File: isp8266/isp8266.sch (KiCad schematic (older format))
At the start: 0 parts

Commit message: Complete power sch
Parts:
- added C? (x4): 10u, symbol Device:C_Small
- added C? (x6): 22u, symbol Device:C_Small
- added C? (x2): 1u, symbol Device:C_Small
- added D? (x2): LED_Small, symbol Device:LED_Small
- added L?: L_Small, symbol Device:L_Small
- added P?: USB_C_Plug, symbol Connector:USB_C_Plug
- added R? (x2): 5k1, symbol Device:R_Small
- added R?: 10k, symbol Device:R_Small
- added R?: 2, symbol Device:R_Small
- added R? (x2): 1k, symbol Device:R_Small
- added R?: 0.9, symbol Device:R_Small
- added SW?: SW_Push, symbol Switch:SW_Push
- added U?: ESP-12E, RF_Module:ESP-12E, symbol RF_Module:ESP-12E
- added U?: AP1117-33, Package_TO_SOT_SMD:SOT-223-3_TabPin2, symbol Regulator_Linear:AP1117-33
- added U?: IPS5306, symbol IPS5306:IPS5306
- added U?: CH340C, Package_SO:SOIC-16_3.9x9.9mm_P1.27mm, symbol Interface_USB:CH340C
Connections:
- new net: D?.2 (A), U?.2 (LED1)
- new net: R?.1, U?.3 (LED2), U?.4 (LED3)
- new net: SW?.1, U?.5 (KEY)
- new net: L?.1, U?.7 (SW)
- new net: P?.A5 (CC), R?.1
- new net: P?.B5 (VCONN), R?.1
- new net: R?.1, SW?.2
- new net: C?.1, R?.2
- new net: D?.1 (K), R?.1
- new net +3V3: C?.1, C?.1, D?.2 (A), U?.2 (VO)
- new net +5V: C?.1, C?.1, C?.1, C?.1, C?.1, C?.1, U?.3 (VI), U?.8 (VOUT)
- new net BAT: C?.1, L?.2, R?.1
- new net D+: P?.A6 (D+)
- new net D-: P?.A7 (D-)
- new net GND: C?.2, C?.2, C?.2, C?.2, C?.2, C?.2, C?.2, C?.2, C?.2, C?.2, C?.2, C?.2, D?.1 (K), P?.A1 (GND), P?.A10 (RX2-), P?.A11 (RX2+), P?.A12 (GND), P?.A2 (TX1+), P?.A3 (TX1-), P?.B1 (GND), P?.B10 (RX1-), P?.B11 (RX1+), P?.B12 (GND), P?.B2 (TX2+), P?.B3 (TX2-), P?.S1 (SHIELD), R?.2, R?.2, R?.2, R?.2, U?.1 (GND), U?.9 (GND)
- new net IC_BAT: C?.1, R?.2, R?.2, U?.6 (BAT)
- new net VBUS: C?.1, P?.A4 (VBUS), P?.A9 (VBUS), P?.B4 (VBUS), P?.B9 (VBUS), R?.1, U?.1 (VIN)
- no-connect marks 0 -> 2

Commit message: Complete all peripherals
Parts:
- added C? (x2): 100n, symbol Device:C_Small
- added C?: 10u, symbol Device:C_Small
- added C?: 470p, symbol Device:C_Small
- added C?: 100p, symbol Device:C_Small
- added J?: S0, symbol Connector_Generic:Conn_01x03
- added J?: S1, symbol Connector_Generic:Conn_01x03
- added J?: S2, symbol Connector_Generic:Conn_01x03
- added J?: S3, symbol Connector_Generic:Conn_01x03
- added J?: IMU, symbol Connector_Generic:Conn_01x04
- added J?: USART, symbol Connector_Generic:Conn_01x04
- added J?: F0, symbol Connector_Generic:Conn_01x02
- added J?: F1, symbol Connector_Generic:Conn_01x02
- added J?: BATTERY, symbol Connector_Generic:Conn_01x02
- added J?: I2C, symbol Connector_Generic:Conn_01x04
- added Q? (x2): S8050, Package_TO_SOT_THT:TO-92_Inline, symbol Transistor_BJT:S8050
- added Q? (x2): IRLML0030, Package_TO_SOT_SMD:SOT-23, symbol Transistor_FET:IRLML0030
- added R? (x2): 470, symbol Device:R_Small
- added R? (x6): 10k, symbol Device:R_Small
- added R? (x2): 4k7, symbol Device:R_Small
- added R? (x4): 1k, symbol Device:R_Small
- L?: value L_Small -> 1u
- R?: value 0.9 -> 0.5
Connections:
- net GND is gone; now on net -BATT: C?.2, C?.2, C?.2, C?.2, C?.2, C?.2, C?.2, C?.2, C?.2, C?.2, C?.2, C?.2, D?.1 (K), P?.A1 (GND), P?.A10 (RX2-), P?.A11 (RX2+), P?.A12 (GND), P?.A2 (TX1+), P?.A3 (TX1-), P?.B1 (GND), P?.B10 (RX1-), P?.B11 (RX1+), P?.B12 (GND), P?.B2 (TX2+), P?.B3 (TX2-), P?.S1 (SHIELD), R?.2, R?.2, R?.2, R?.2, U?.1 (GND), U?.9 (GND)
- net +3V3: now also U?.16 (VCC), U?.8 (VCC), C?.1, C?.1, C?.1, J?.1 (Pin_1), J?.1 (Pin_1), J?.1 (Pin_1), R?.2, R?.2, R?.2, R?.2
- net +5V: now also J?.1 (Pin_1), J?.1 (Pin_1), J?.1 (Pin_1), J?.1 (Pin_1)
- net D+: now also U?.5 (UD+)
- net D-: now also U?.6 (UD-)
- net RST: now reaches U?.1 (~RST)
- net RST: now also C?.2, Q?.3 (C), R?.1
- net -BATT: now reaches U?.15 (GND)
- net -BATT: now also U?.1 (GND), C?.1, C?.2, C?.2, C?.2, C?.2, J?.2 (Pin_2), J?.2 (Pin_2), J?.3 (Pin_3), J?.3 (Pin_3), J?.3 (Pin_3), J?.3 (Pin_3), J?.4 (Pin_4), J?.4 (Pin_4), Q?.2 (S), Q?.2 (S), R?.1, R?.1
- net GPIO15: now reaches U?.16 (GPIO15)
- net GPIO15: now also Q?.1 (G), R?.2
- net IO2: now reaches U?.17 (GPIO2)
- net IO2: now also R?.1, R?.2
- net IO0: now reaches U?.18 (GPIO0)
- net IO0: now also Q?.3 (C), R?.1, R?.2
- net SDA: now reaches U?.19 (GPIO4)
- net SDA: now also J?.2 (Pin_2), J?.4 (Pin_4)
- net SCL: now reaches U?.20 (GPIO5)
- net SCL: now also J?.3 (Pin_3), J?.3 (Pin_3)
- net TXD: now reaches U?.21 (GPIO3/RXD)
- net TXD: now also J?.3 (Pin_3), R?.1
- net RXD: now reaches U?.22 (GPIO1/TXD)
- net RXD: now also J?.2 (Pin_2), R?.1
- net EN: now reaches U?.3 (EN)
- net EN: now also R?.1
- net GPIO14: now reaches U?.5 (GPIO14)
- net GPIO14: now also Q?.1 (G), R?.2
- net GPIO12: now reaches U?.6 (GPIO12)
- net GPIO12: now also R?.2
- net GPIO13: now reaches U?.7 (GPIO13)
- net GPIO13: now also R?.2
- net at U?.13 (~DTR): now also Q?.1 (E), R?.1
- net at U?.14 (~RTS): now also Q?.1 (E), R?.1
- net at U?.2 (TXD): now also R?.2
- net at U?.3 (RXD): now also R?.2
- net at U?.4 (V3): now also C?.1
- net BAT renamed +BATT
- net +BATT: now also J?.1 (Pin_1), J?.1 (Pin_1), J?.1 (Pin_1)
- new net: Q?.2 (B), R?.2 (x2)
- new net: J?.2 (Pin_2), R?.1 (x4)
- new net: J?.2 (Pin_2), Q?.3 (D) (x2)
- no-connect marks 2 -> 15
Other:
- note added: "5V to 3V3"
- note added: "Battery"
- note added: "ESP8266"
- note added: "Fire"
- note added: "Peripherals"
- note added: "USB C Power Supply"
- note added: "USB TTL"
- moved on the sheet: C?, D?, L?, P?, R?, SW?, U?, U?A

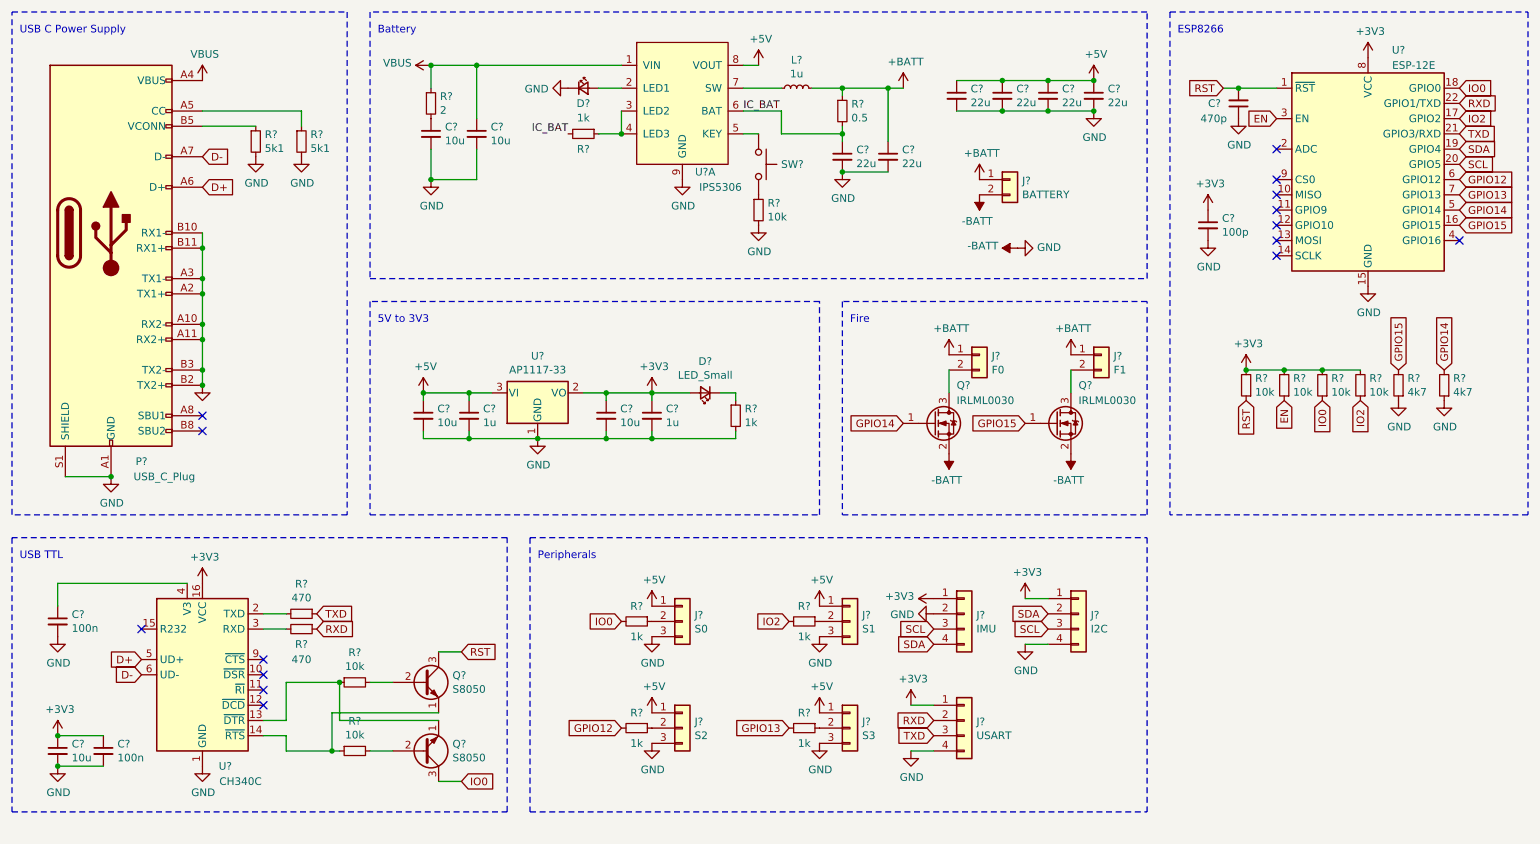
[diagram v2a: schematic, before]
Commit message: Annotate all symbols
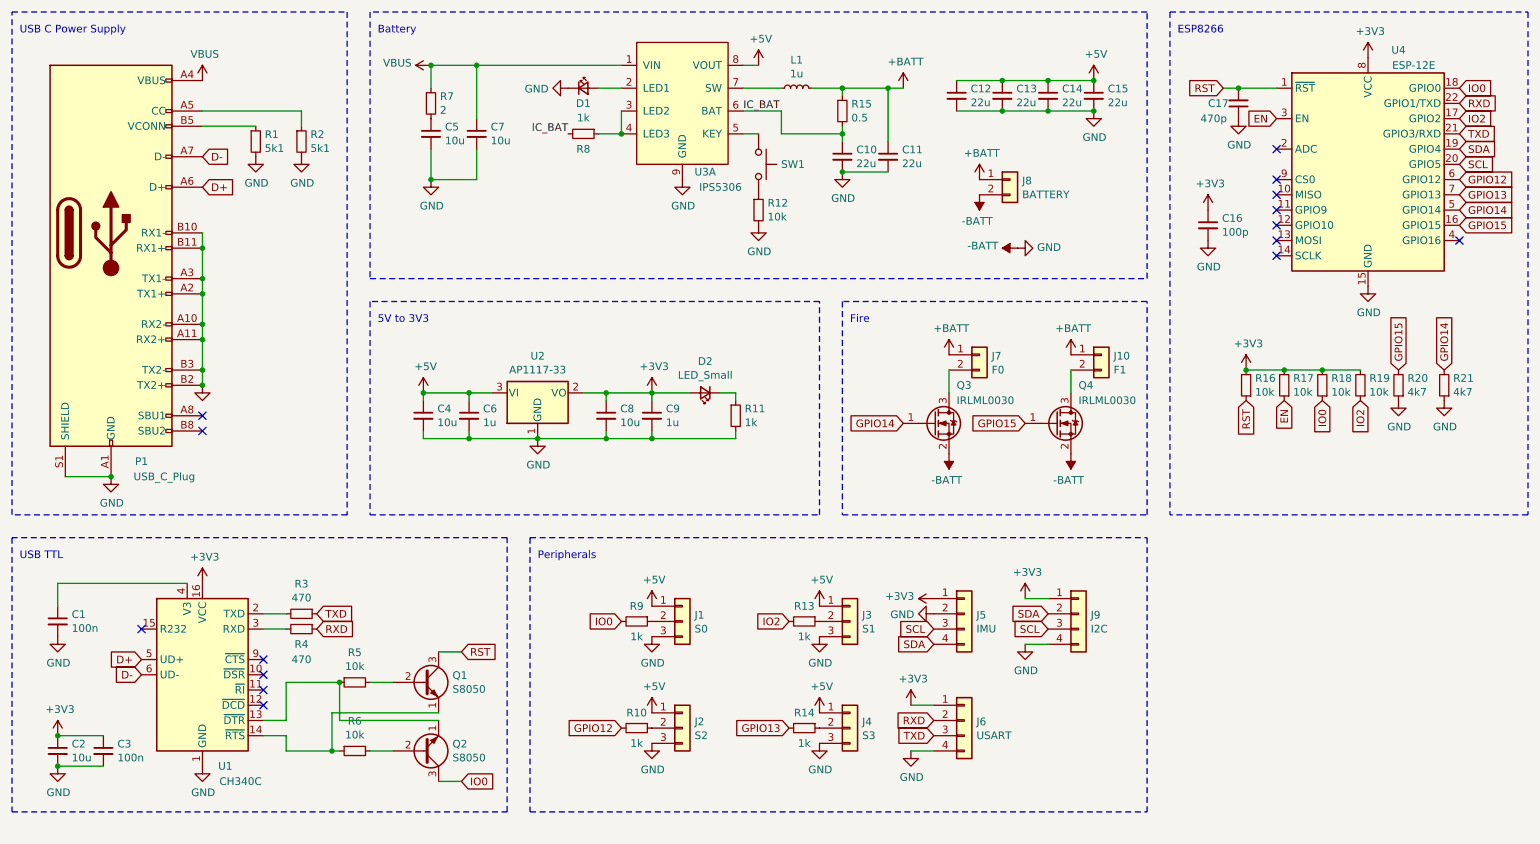
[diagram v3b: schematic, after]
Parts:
- gave numbers to parts that had none: 61

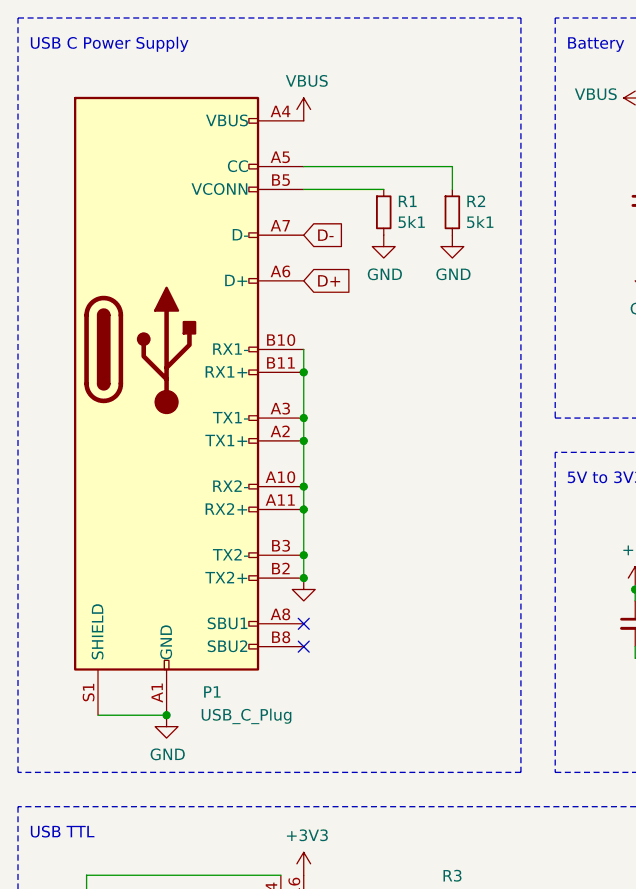
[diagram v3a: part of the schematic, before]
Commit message: Use USB_C_Receptacle
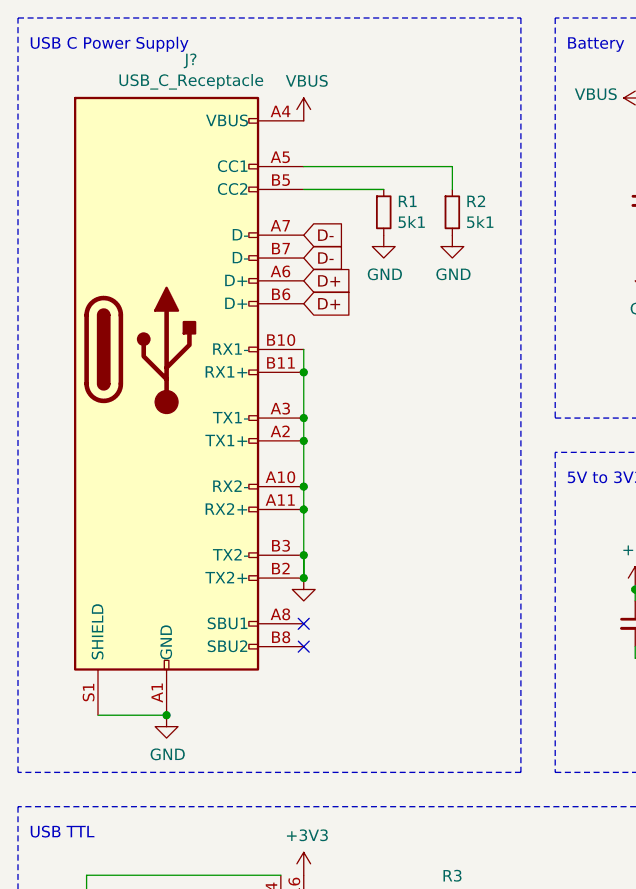
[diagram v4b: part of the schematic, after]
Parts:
- removed P1: USB_C_Plug, symbol Connector:USB_C_Plug
- added J?: USB_C_Receptacle, symbol Connector:USB_C_Receptacle
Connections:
- net -BATT: now also J?.A1 (GND), J?.A10 (RX2-), J?.A11 (RX2+), J?.A12 (GND), J?.A2 (TX1+), J?.A3 (TX1-), J?.B1 (GND), J?.B10 (RX1-), J?.B11 (RX1+), J?.B12 (GND), J?.B2 (TX2+), J?.B3 (TX2-), J?.S1 (SHIELD)
- net D+: now also J?.A6 (D+), J?.B6 (D+)
- net D-: now also J?.A7 (D-), J?.B7 (D-)
- net VBUS: now also J?.A4 (VBUS), J?.A9 (VBUS), J?.B4 (VBUS), J?.B9 (VBUS)
- net at R2.1: now also J?.A5 (CC1)
- net at R1.1: now also J?.B5 (CC2)
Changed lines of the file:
@@
 Comment4 ""
 $EndDescr
-$Comp
-L Connector:USB_C_Plug P1
-U 1 1 638029CF
-P 1300 2050
-F 0 "P1" H 1500 550 50  0000 C CNN
-F 1 "USB_C_Plug" H 1650 450 50  0000 C CNN
-F 2 "" H 1450 2050 50  0001 C CNN
-F 3 "https://www.usb.org/sites/default/files/documents/usb_type-c.zip" H 1450 2050 50  0001 C CNN
-	1    1300 2050
-	1    0    0    -1
-$EndComp
 Text GLabel 1900 1750 2    50   Input ~ 0
 D+
@@
 	1    0    0    -1
 $EndComp
-Connection ~ 1300 3650
-Wire Wire Line
-	1900 2050 1900 2150
-Connection ~ 1900 2150
-Wire Wire Line
-	1900 2150 1900 2350
-Connection ~ 1900 2350
-Wire Wire Line
-	1900 2350 1900 2450
-Connection ~ 1900 2450
-Wire Wire Line
-	1900 2450 1900 2650
-Connection ~ 1900 2650
-Wire Wire Line
-	1900 2650 1900 2750
-Connection ~ 1900 2750
-Wire Wire Line
-	1900 2750 1900 2950
-Connection ~ 1900 2950
-Wire Wire Line
-	1900 2950 1900 3050
 $Comp
 L Device:R_Small R1
@@
 	1    0    0    -1
 $EndComp
-Connection ~ 1900 3050
 NoConn ~ 1900 3250
 NoConn ~ 1900 3350
@@
 $EndComp
 $Comp
+L power:GND #PWR01
+U 1 1 63C8E842
+P 950 4700
+F 0 "#PWR01" H 950 4450 50  0001 C CNN
+F 1 "GND" H 955 4527 50  0000 C CNN
+F 2 "" H 950 4700 50  0001 C CNN
+F 3 "" H 950 4700 50  0001 C CNN
+	1    950  4700
+	1    0    0    -1
+$EndComp
+Wire Wire Line
+	1800 4350 950  4350
+Wire Wire Line
+	950  4350 950  4500
+$Comp
 L Device:C_Small C1
 U 1 1 63C8D629
@@
 $EndComp
 $Comp
-L power:GND #PWR01
-U 1 1 63C8E842
-P 950 4700
-F 0 "#PWR01" H 950 4450 50  0001 C CNN
-F 1 "GND" H 955 4527 50  0000 C CNN
-F 2 "" H 950 4700 50  0001 C CNN
-F 3 "" H 950 4700 50  0001 C CNN
-	1    950  4700
-	1    0    0    -1
-$EndComp
-Wire Wire Line
-	1800 4350 950  4350
-Wire Wire Line
-	950  4350 950  4500
+L Connector:USB_C_Receptacle J?
+U 1 1 63C95E22
+P 1300 2050
+F 0 "J?" H 1407 3317 50  0000 C CNN
+F 1 "USB_C_Receptacle" H 1407 3226 50  0000 C CNN
+F 2 "" H 1450 2050 50  0001 C CNN
+F 3 "https://www.usb.org/sites/default/files/documents/usb_type-c.zip" H 1450 2050 50  0001 C CNN
+	1    1300 2050
+	1    0    0    -1
+$EndComp
+Connection ~ 1300 3650
+Wire Wire Line
+	1900 2950 1900 3050
+Connection ~ 1900 3050
+Wire Wire Line
+	1900 2050 1900 2150
+Connection ~ 1900 2150
+Wire Wire Line
+	1900 2150 1900 2350
+Connection ~ 1900 2350
+Wire Wire Line
+	1900 2350 1900 2450
+Connection ~ 1900 2450
+Wire Wire Line
+	1900 2450 1900 2650
+Connection ~ 1900 2650
+Wire Wire Line
+	1900 2650 1900 2750
+Connection ~ 1900 2750
+Wire Wire Line
+	1900 2750 1900 2950
+Connection ~ 1900 2950
+Wire Wire Line
+	1900 2950 1900 3050
+Text GLabel 1900 1650 2    50   Input ~ 0
+D-
+Text GLabel 1900 1850 2    50   Input ~ 0
+D+
 $EndSCHEMATC

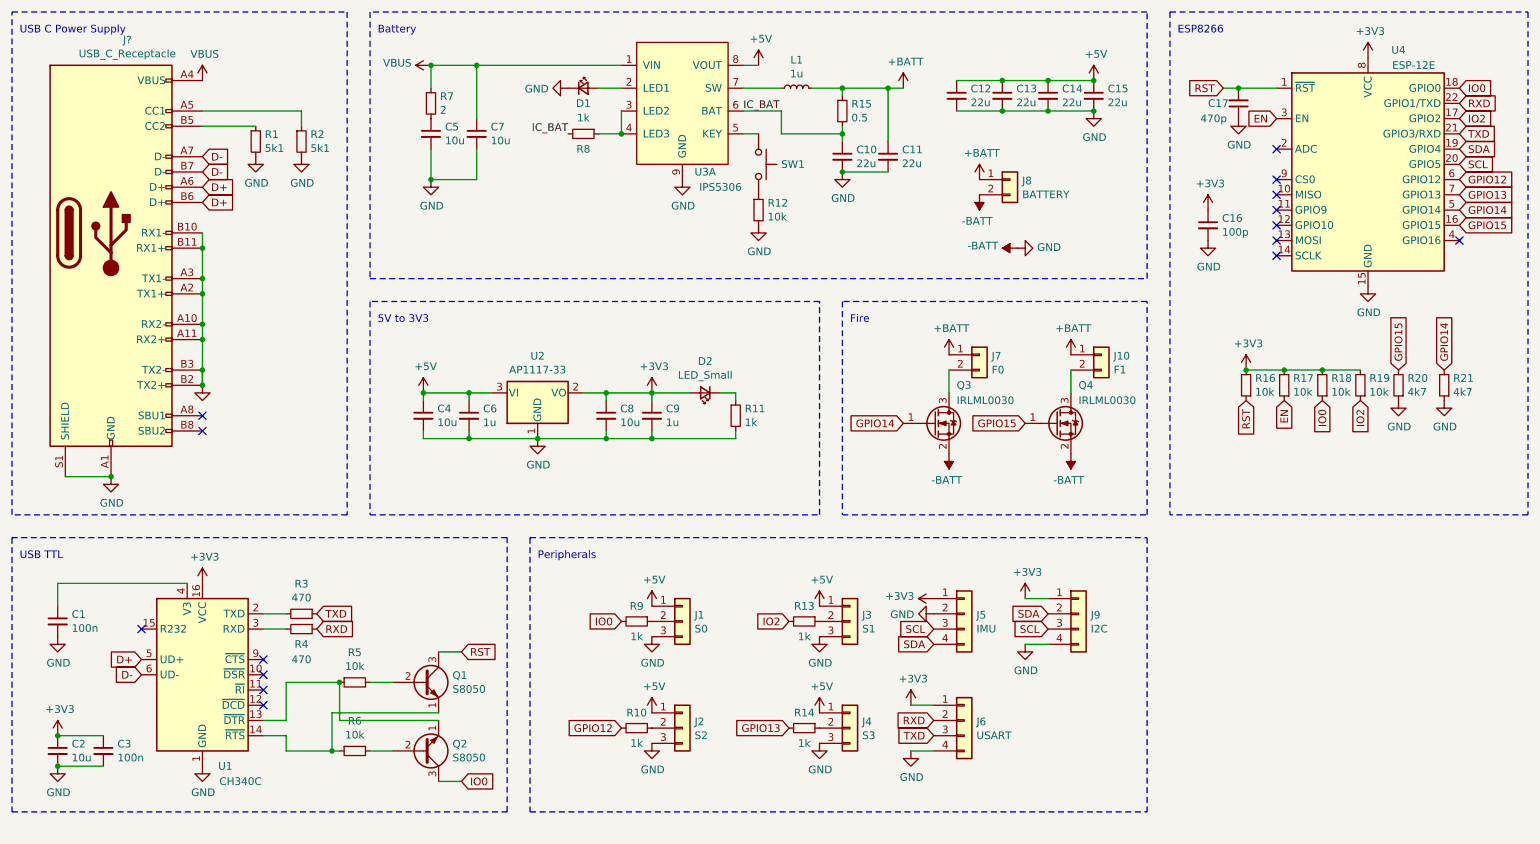
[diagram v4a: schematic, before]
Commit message: Modify some components' position
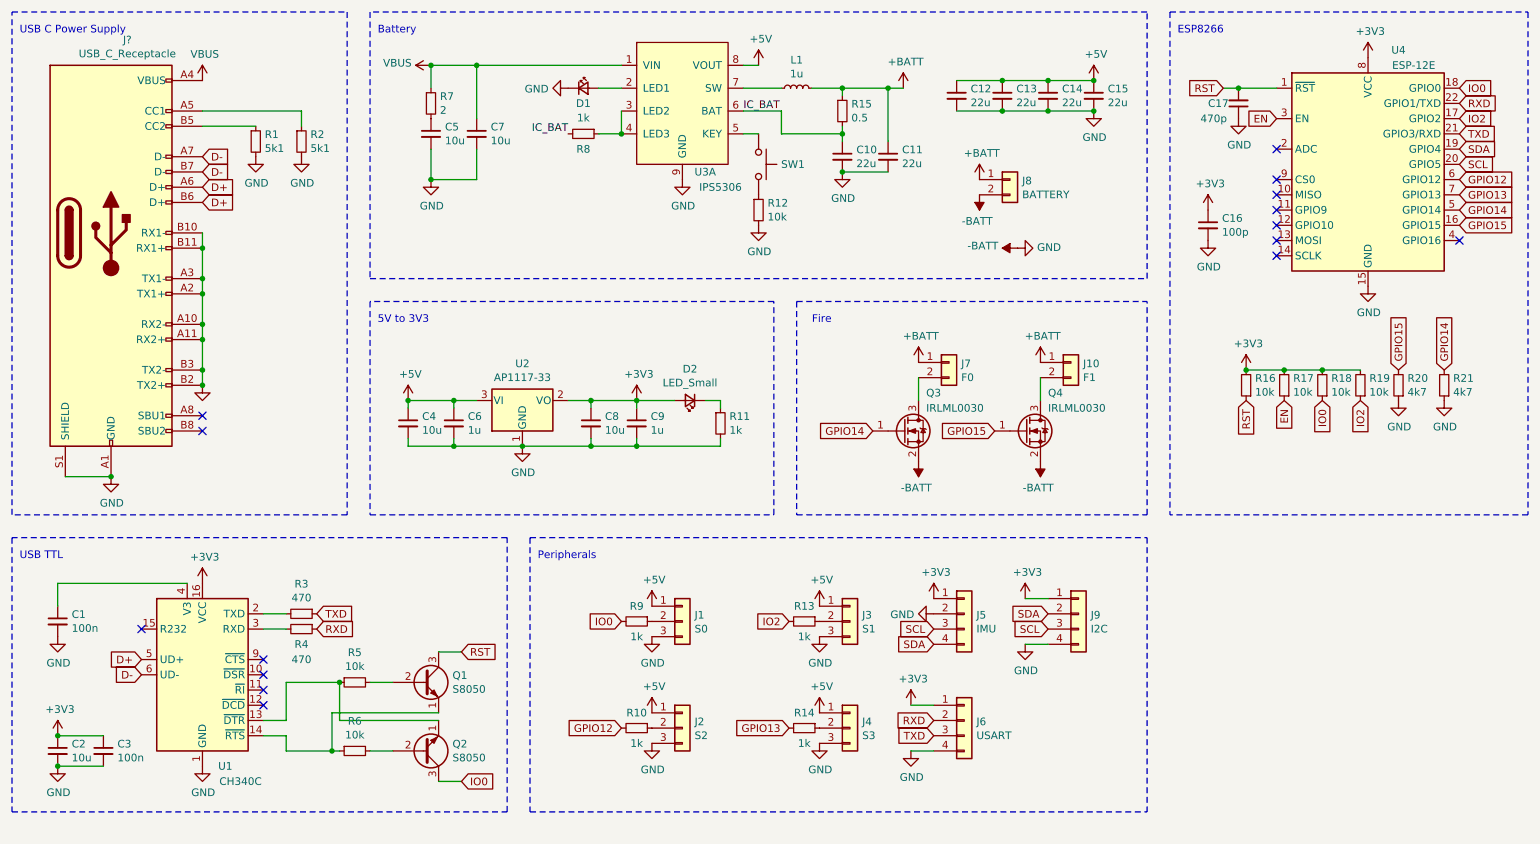
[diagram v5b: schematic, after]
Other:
- moved on the sheet: C4, C6, C8, C9, D2, J10, J7, Q3, Q4, R11, U2
